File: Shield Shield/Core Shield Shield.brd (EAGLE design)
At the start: 115.6 x 54.6 mm, 7 parts

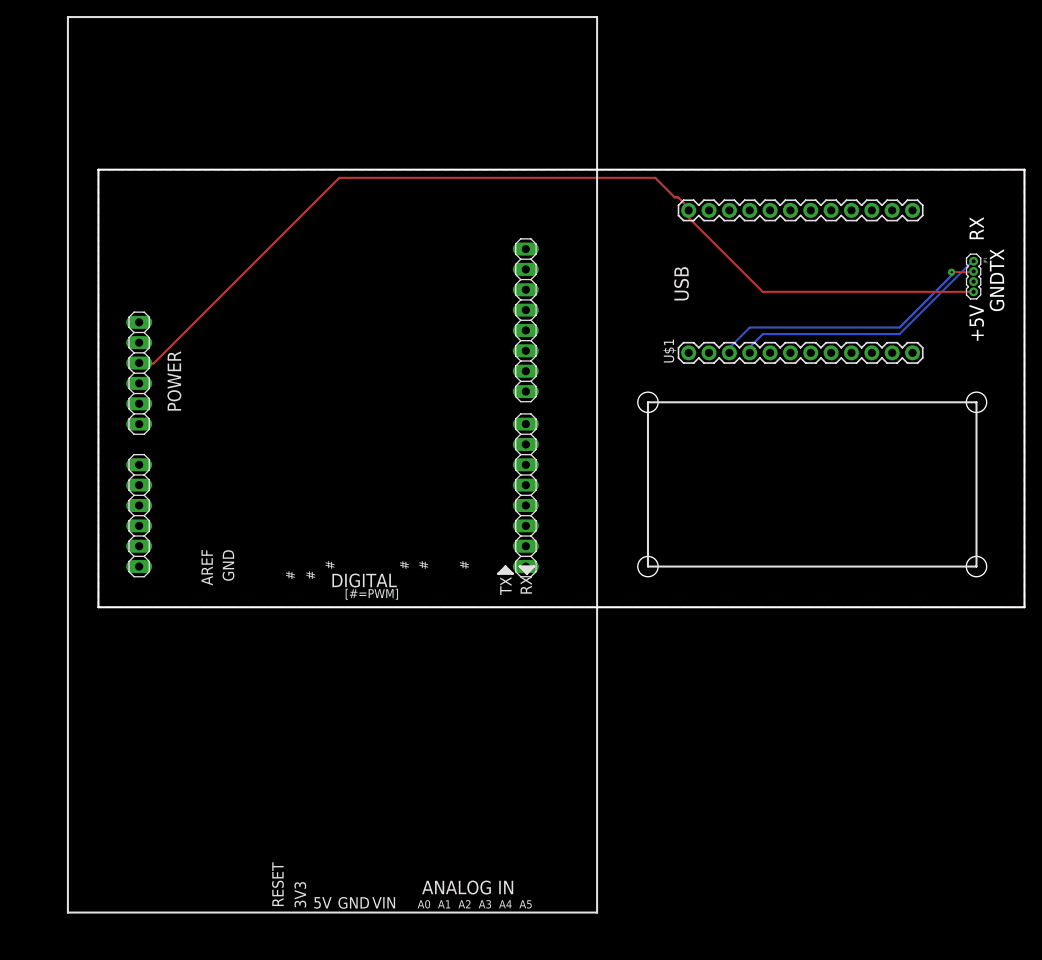
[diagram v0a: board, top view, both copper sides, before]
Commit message: Brought in the correct Shield Shield EAGLE files
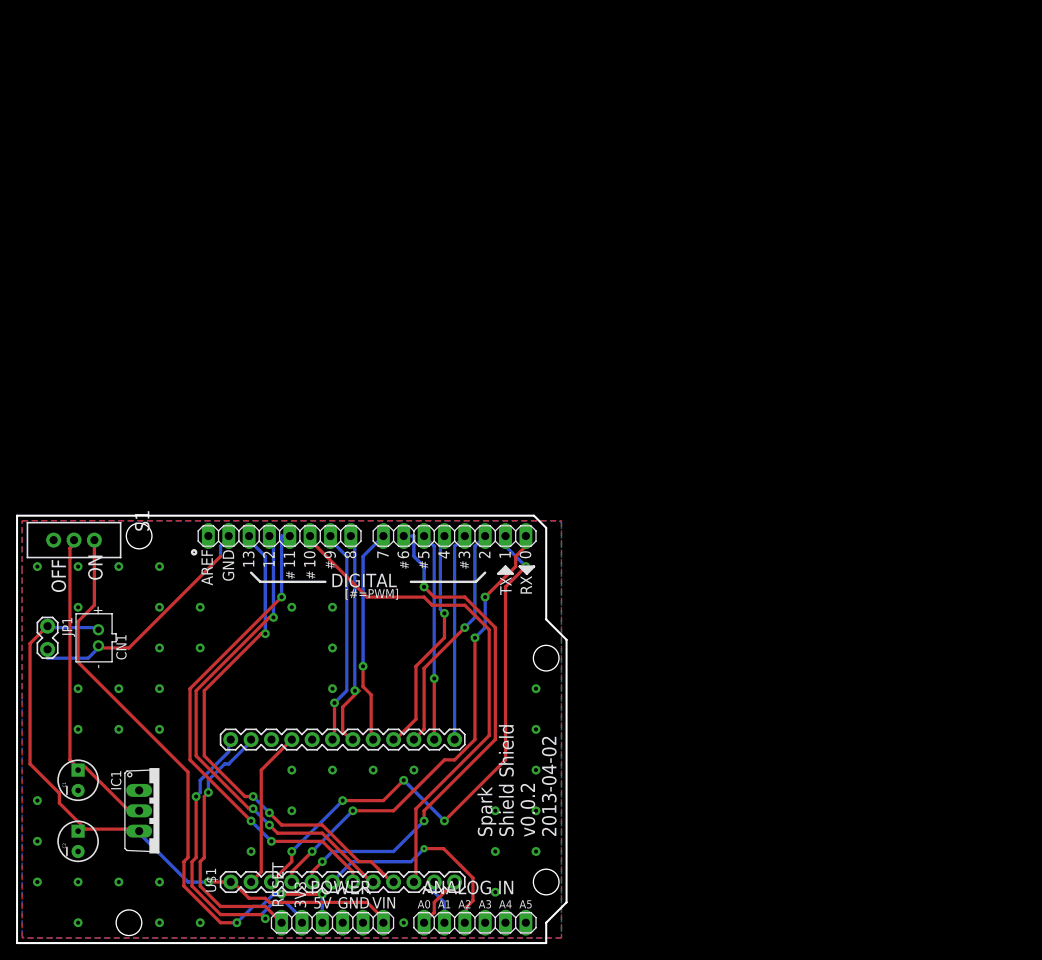
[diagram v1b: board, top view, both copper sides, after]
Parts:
- added C1: 10uF, SparkFun-Capacitors:CPOL-RADIAL-10UF-25V
- added C2: 1uF, SparkFun-Capacitors:CPOL-RADIAL-10UF-25V
- added CN1: (no value), adafruit:JST-PH-2-THM
- added IC1: MC33269T-5.0, linear:TO220V
- added S1: (no value), SparkFun-Electromechanical:SWITCH-SPDT
- JP1: device SparkFun-Connectors:1X04-1.27MM -> SparkFun-Connectors:1X02_LOCK
- moved JP1 124.3 mm to (3.81, 39.4)
- moved U$1 87.3 mm to (40.6, 16.5)
- moved POWER 72.7 mm to (39.4, 2.54), turned to 0 degrees
- moved AD 65.9 mm to (57.1, 2.54), turned to 0 degrees
- moved IOH 40.9 mm to (32.8, 50.8), turned to 180 degrees
- moved IOL 10.2 mm to (54.6, 50.8), turned to 180 degrees
- moved U$2 7.41 mm to (1.27, 1.27)
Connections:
- removed net RAW: U$1.1
- removed net RX: JP1.1, U$1.4
- removed net TX: JP1.2, U$1.3
- new net +3V3: POWER.2, U$1.24
- new net AD0: AD.1, U$1.12
- new net AD1: AD.2, U$1.11
- new net AD2: AD.3, U$1.6
- new net IO0: IOL.1, U$1.4
- new net IO1: IOL.2, U$1.3
- new net IO2: IOL.3, U$1.15
- new net IO3: IOL.4, U$1.13
- new net IO4: IOL.5, U$1.16
- new net IO5: IOL.6, U$1.14
- new net IO6: IOL.7, U$1.5
- new net IO7: IOL.8, U$1.17
- new net IO8: IOH.1, U$1.18
- new net IO9: IOH.2, U$1.19
- new net MISO: IOH.5, U$1.8
- new net MOSI: IOH.4, U$1.7
- new net N1: C1.1, IC1.2, S1.2
- new net RESET: POWER.1, U$1.23
- new net SCK: IOH.6, U$1.9
- new net SS: IOH.3, U$1.10
- new net VIN: C2.1, CN1.1, IC1.3, JP1.1, POWER.6, U$1.1
- net +5V: now also S1.1; no longer JP1.4, U$1.24
- net GND: now also C1.2, C2.2, CN1.2, IC1.1, JP1.2; no longer JP1.3
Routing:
- net VIN: track 0.00 -> 79.5 mm, vias 0 -> 1
- net IO1: track 0.00 -> 70.5 mm, vias 0 -> 5
- net IO6: track 0.00 -> 64.8 mm, vias 0 -> 3
- net SS: track 0.00 -> 63.0 mm
- net SCK: track 0.00 -> 61.9 mm, vias 0 -> 3
- net MOSI: track 0.00 -> 61.3 mm, vias 0 -> 3
- net MISO: track 0.00 -> 60.6 mm, vias 0 -> 3
- net IO0: track 0.00 -> 59.0 mm, vias 0 -> 4
- net GND: track 0.00 -> 51.9 mm, vias 0 -> 43
- net +5V: track 120.9 -> 74.1 mm, vias 0 -> 3
- net N1: track 0.00 -> 39.5 mm
- net +3V3: track 0.00 -> 39.0 mm, vias 0 -> 2
- net TX: track 35.5 -> 0.00 mm, vias 1 -> 0
- net RESET: track 0.00 -> 33.6 mm, vias 0 -> 1
- net RX: track 33.1 -> 0.00 mm
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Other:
- board size 115.6 x 54.6 mm -> 68.6 x 53.3 mm
- board text added: "0"
- board text added: "1"
- board text added: "10"
- board text added: "11"
- board text added: "12"
- board text added: "13"
- board text added: "2"
- board text added: "3"
- board text added: "4"
- board text added: "5"
- board text added: "6"
- board text added: "7"
- board text added: "8"
- board text added: "9"
- board text added: "OFF"
- board text added: "ON"
- board text added: "Spark Shield Shield v0.0.2 2013-04-02"
- board text removed: "+5V"
- board text removed: "USB"

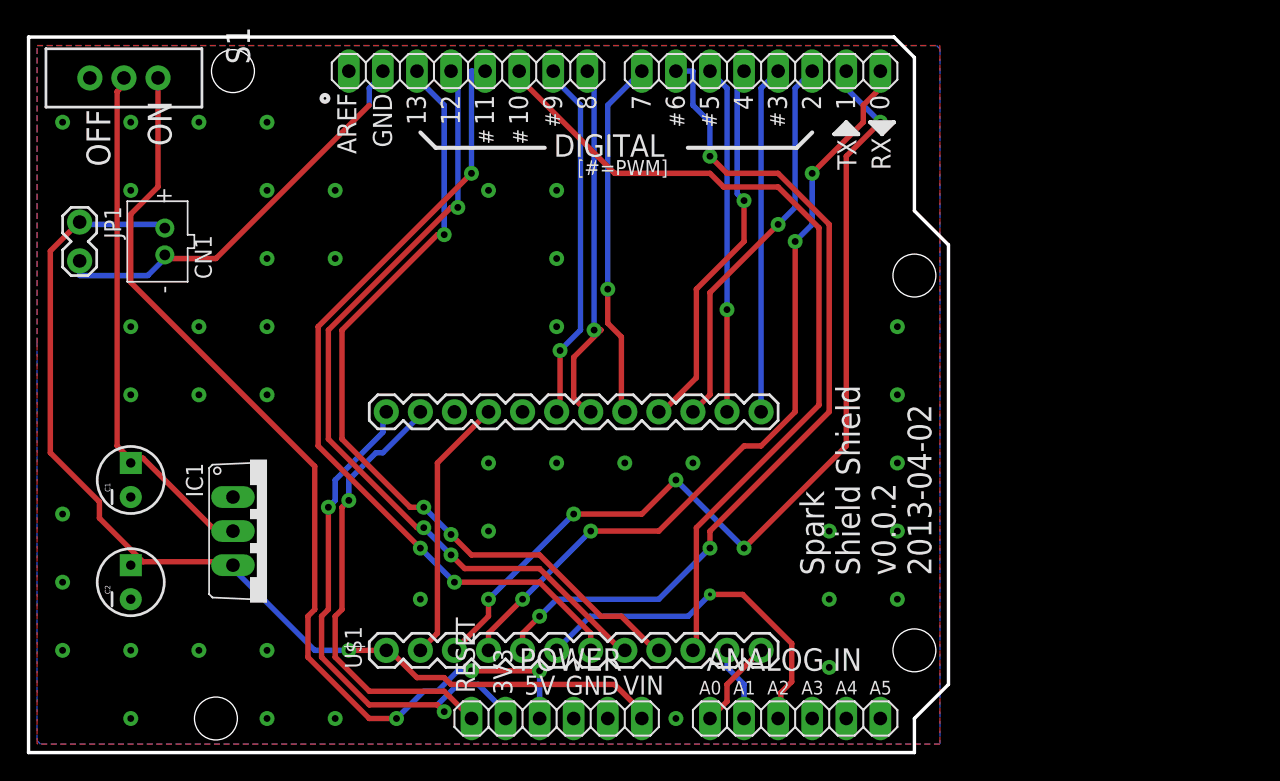
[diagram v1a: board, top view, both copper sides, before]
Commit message: Updated Shield Shield so Core is not underneath Shield
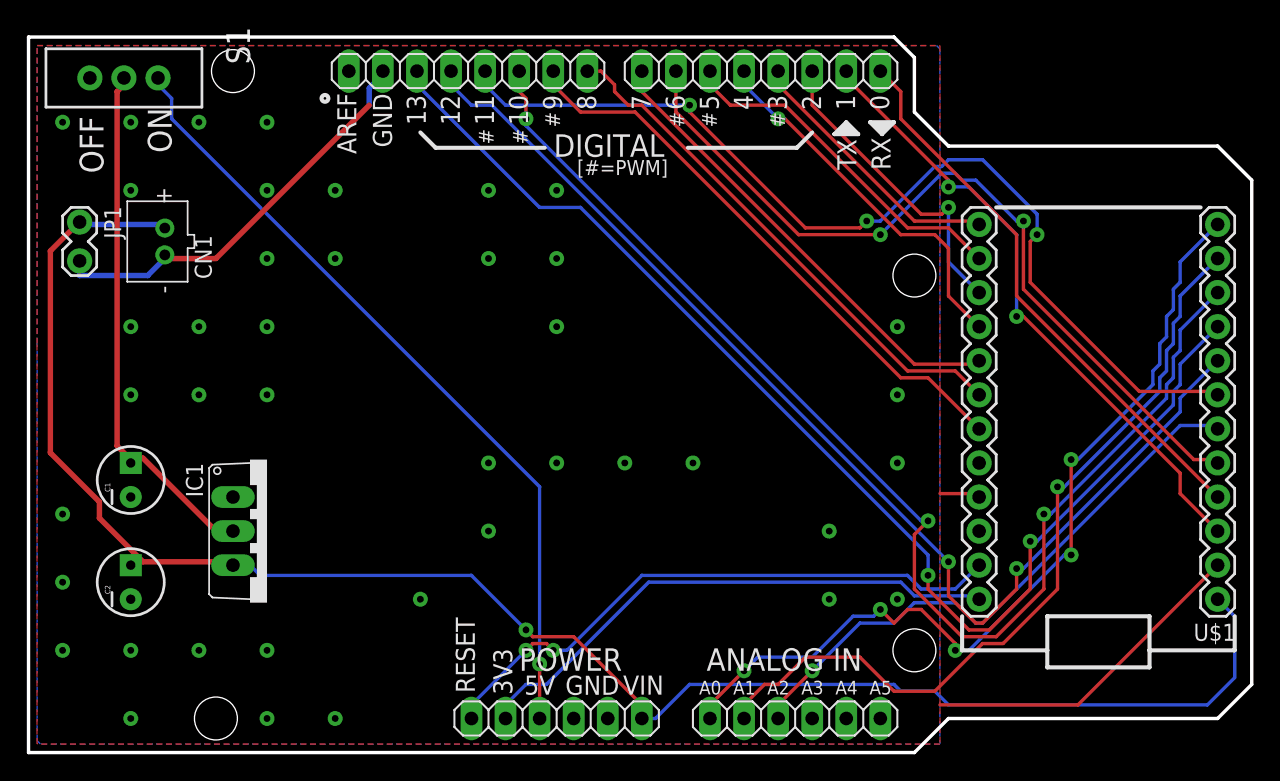
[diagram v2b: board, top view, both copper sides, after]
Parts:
- moved U$1 40.1 mm to (79.8, 25.4), turned to 180 degrees
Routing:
- net AD0: track 6.66 -> 65.7 mm, vias 0 -> 5
- net AD1: track 5.61 -> 59.9 mm, vias 0 -> 1
- net VIN: track 79.5 -> 132.9 mm
- net SCK: track 61.9 -> 93.0 mm, vias 3 -> 2
- net SS: track 63.0 -> 93.2 mm, vias 0 -> 3
- net MISO: track 60.6 -> 85.9 mm, vias 3 -> 2
- net IO1: track 70.5 -> 46.9 mm, vias 5 -> 2
- net AD2: track 26.8 -> 43.8 mm
- net IO0: track 59.0 -> 42.2 mm, vias 4 -> 0
- net IO9: track 27.1 -> 43.4 mm, vias 1 -> 0
- net +5V: track 74.1 -> 59.5 mm, vias 3 -> 1
- net MOSI: track 61.3 -> 73.7 mm
- net IO8: track 27.6 -> 39.5 mm, vias 1 -> 0
- net RESET: track 33.6 -> 44.4 mm, vias 1 -> 2
- net GND: track 51.9 -> 60.0 mm, vias 43 -> 41
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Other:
- board size 68.6 x 53.3 mm -> 91.2 x 53.3 mm
